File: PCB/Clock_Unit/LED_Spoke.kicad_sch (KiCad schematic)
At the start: 4 parts

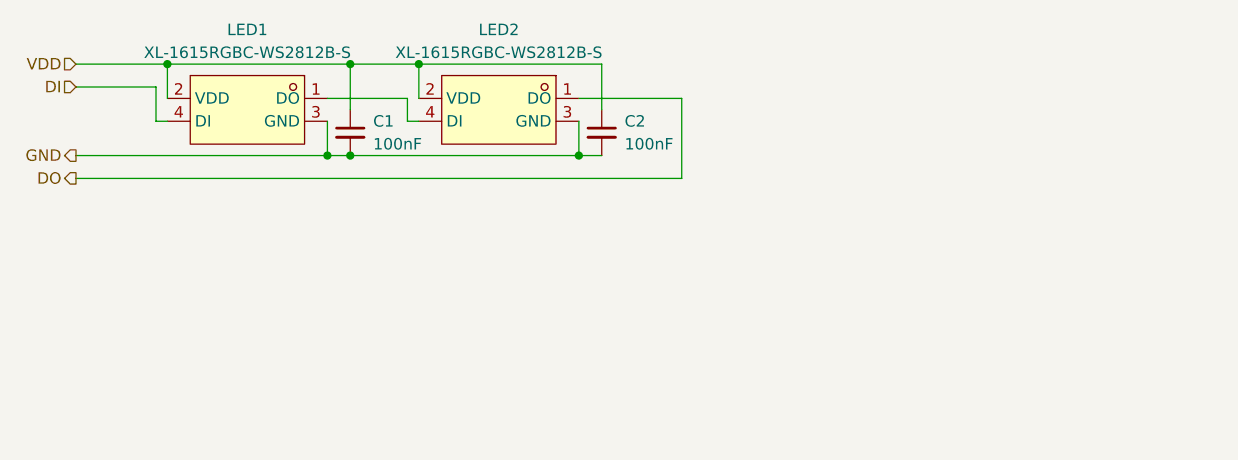
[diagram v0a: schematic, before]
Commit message: Schematic + PCB Updates
Corrected LED symbol and improved silkscreen
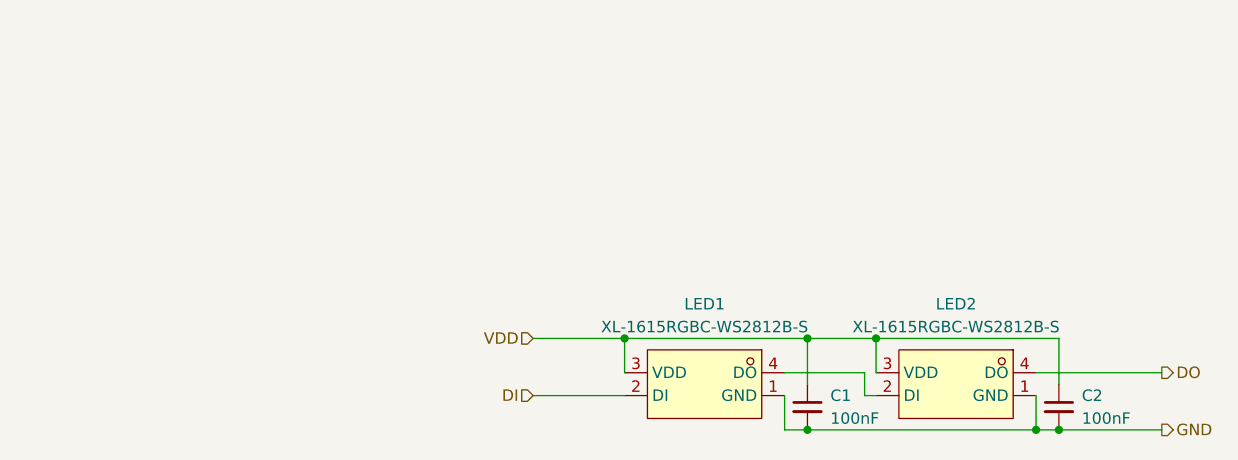
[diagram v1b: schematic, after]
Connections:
- net DI: now also LED1.2 (DI); no longer LED1.4 (DI)
- net DO: now also LED2.4 (DO); no longer LED2.1 (DO)
- net GND: now also LED1.1 (GND), LED2.1 (GND); no longer LED1.3 (GND), LED2.3 (GND)
- net VDD: now also LED1.3 (VDD), LED2.3 (VDD); no longer LED1.2 (VDD), LED2.2 (VDD)
- new net: LED1.4 (DO), LED2.2 (DI)
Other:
- moved on the sheet: C1, C2, LED1, LED2
